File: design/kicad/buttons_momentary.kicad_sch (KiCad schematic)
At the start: 18 parts, among them J2 Conn_01x02_Socket, J3 Conn_01x02_Socket, J4 Conn_01x02_Socket, J5 Conn_01x02_Socket, J6 Conn_01x02_Socket, J7 Conn_01x02_Socket

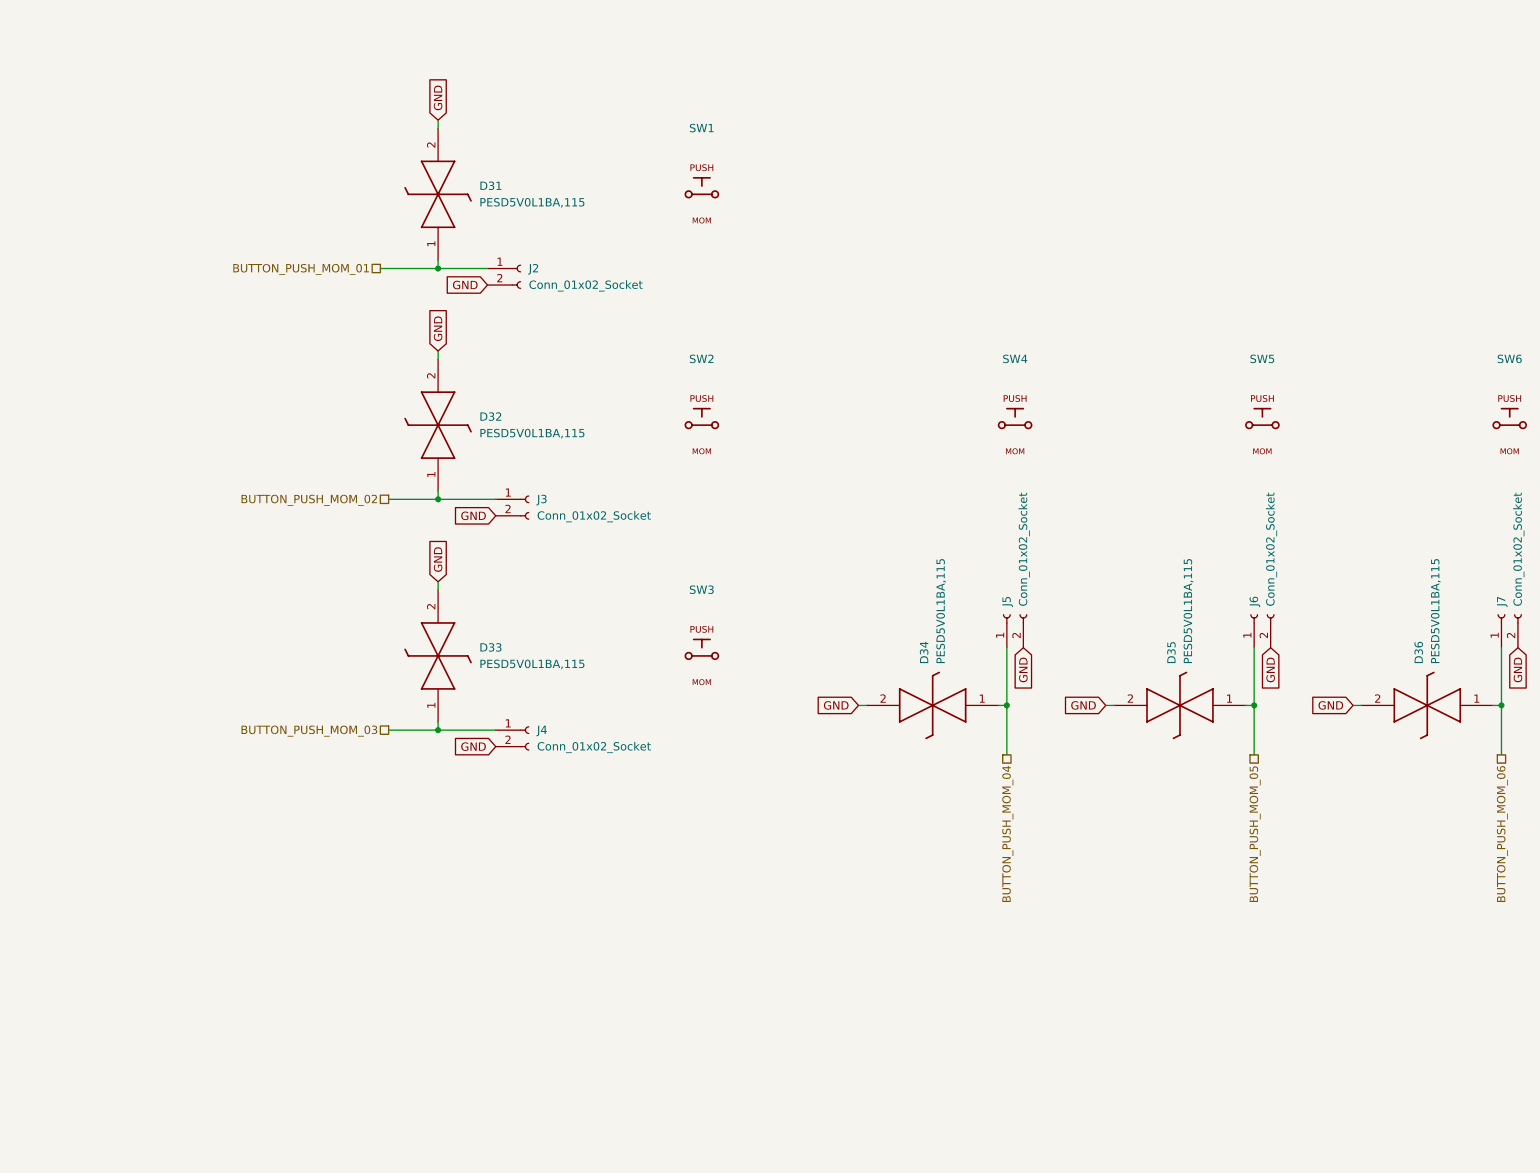
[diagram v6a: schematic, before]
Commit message: Fix net format name and update junctions in MIDI controller schematic
- Set net format name to "KiCad" in the project file.
- Added multiple junctions at specified coordinates in the schematic.
- Adjusted existing junction positions and UUIDs for consistency.
- Updated wire connections to reflect new junction placements.
- Corrected component references and properties for various components.
- Added new capacitor symbols with appropriate properties and references.
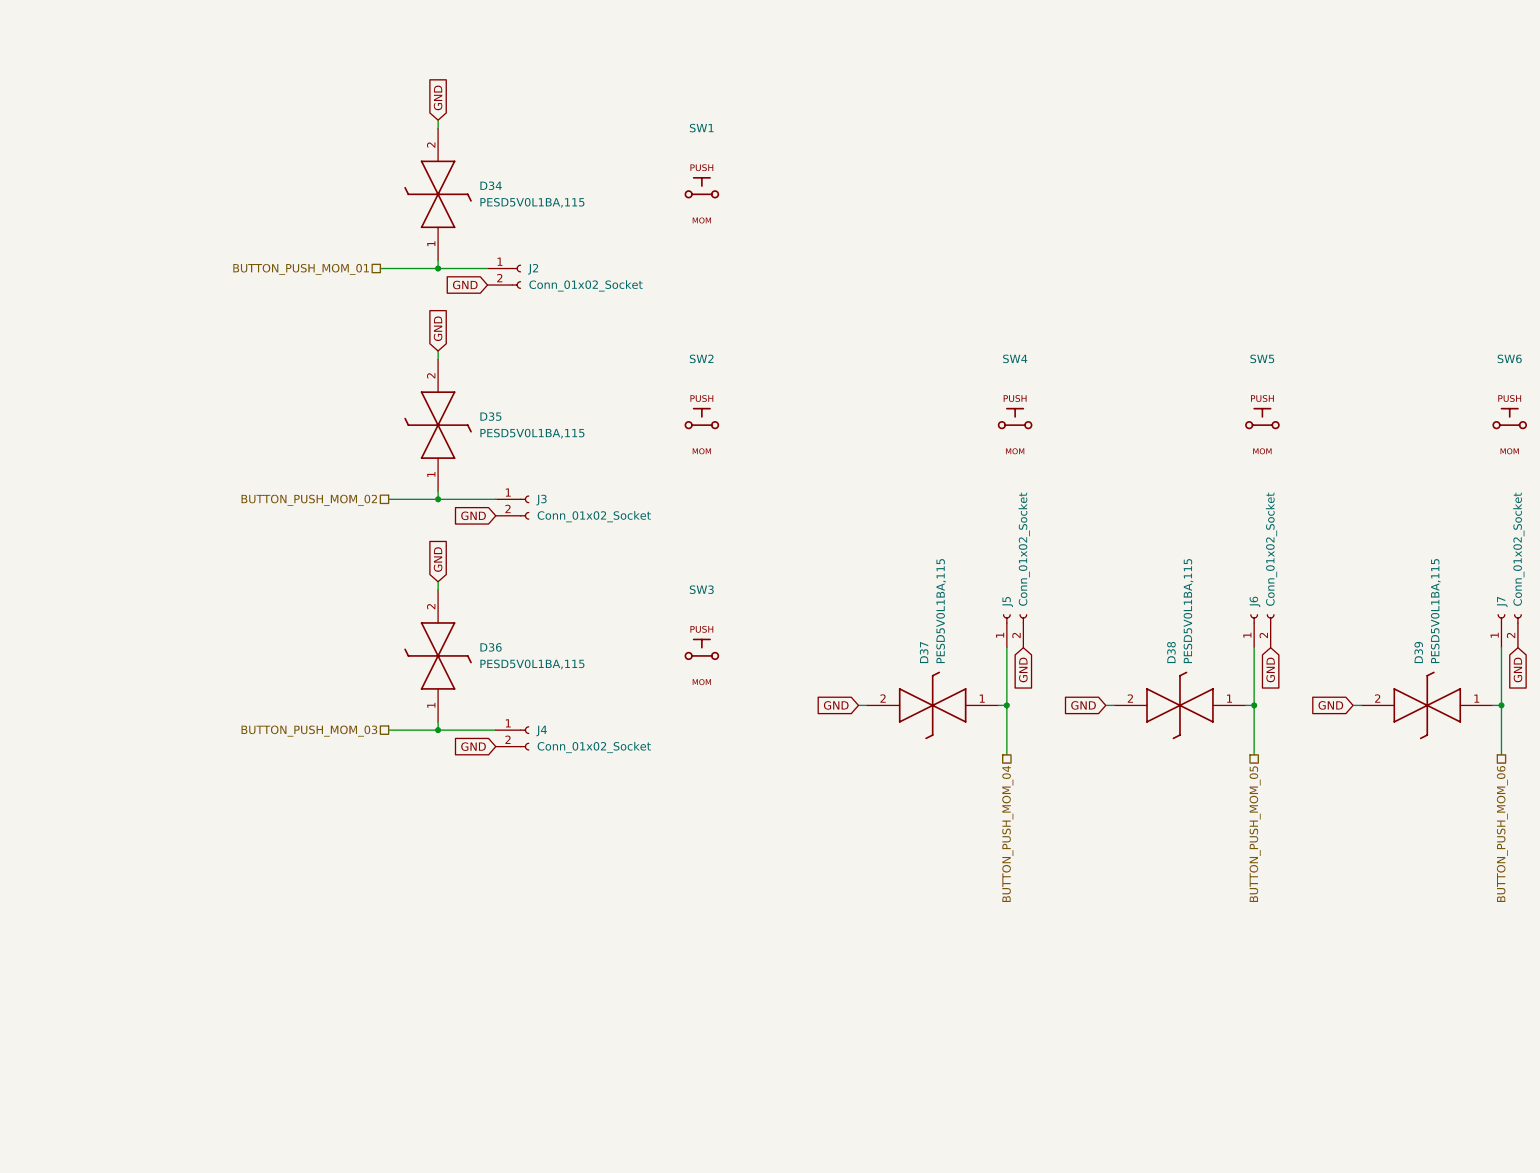
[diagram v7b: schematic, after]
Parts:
- renumbered D31 to D34, D32 to D35, D33 to D36, D34 to D37, D35 to D38, D36 to D39
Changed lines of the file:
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@@
 		(dnp no)
 		(fields_autoplaced yes)
-		(property "Reference" "D35"
+		(property "Reference" "D38"
 			(at 181.6099 114.3 90)
 			(effects
@@
 			(project "midi_controller"
 				(path "/9e44e663-00d0-4f33-bf1f-c4ad78deb554/9031f441-b35d-4c72-b3de-1ac6f4fd634b"
-					(reference "D35")
+					(reference "D38")
 					(unit 1)
 				)
@@
 		(dnp no)
 		(fields_autoplaced yes)
-		(property "Reference" "D32"
+		(property "Reference" "D35"
 			(at 74.93 76.1999 90)
 			(effects
@@
 			(project "midi_controller"
 				(path "/9e44e663-00d0-4f33-bf1f-c4ad78deb554/9031f441-b35d-4c72-b3de-1ac6f4fd634b"
-					(reference "D32")
+					(reference "D35")
 					(unit 1)
 				)
@@
 		(dnp no)
 		(fields_autoplaced yes)
-		(property "Reference" "D31"
+		(property "Reference" "D34"
 			(at 74.93 40.6399 90)
 			(effects
@@
 			(project "midi_controller"
 				(path "/9e44e663-00d0-4f33-bf1f-c4ad78deb554/9031f441-b35d-4c72-b3de-1ac6f4fd634b"
-					(reference "D31")
+					(reference "D34")
 					(unit 1)
 				)
@@
 		(dnp no)
 		(fields_autoplaced yes)
-		(property "Reference" "D34"
+		(property "Reference" "D37"
 			(at 143.5099 114.3 90)
 			(effects
@@
 			(project "midi_controller"
 				(path "/9e44e663-00d0-4f33-bf1f-c4ad78deb554/9031f441-b35d-4c72-b3de-1ac6f4fd634b"
-					(reference "D34")
+					(reference "D37")
 					(unit 1)
 				)
@@
 		(dnp no)
 		(fields_autoplaced yes)
-		(property "Reference" "D36"
+		(property "Reference" "D39"
 			(at 219.7099 114.3 90)
 			(effects
@@
 			(project "midi_controller"
 				(path "/9e44e663-00d0-4f33-bf1f-c4ad78deb554/9031f441-b35d-4c72-b3de-1ac6f4fd634b"
-					(reference "D36")
+					(reference "D39")
 					(unit 1)
 				)
@@
 		(dnp no)
 		(fields_autoplaced yes)
-		(property "Reference" "D33"
+		(property "Reference" "D36"
 			(at 74.93 111.7599 90)
 			(effects
@@
 			(project "midi_controller"
 				(path "/9e44e663-00d0-4f33-bf1f-c4ad78deb554/9031f441-b35d-4c72-b3de-1ac6f4fd634b"
-					(reference "D33")
-					(unit 1)
-				)
+					(reference "D36")
+					(unit 1)
+				)

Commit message: Fix reference labels and update wire connections in MIDI controller and multiplexer schematics
- Adjusted wire connection points in the MIDI controller schematic for better alignment.
- Updated label positions for various components in the MIDI controller schematic.
- Renamed reference designators for capacitors and power connections in the multiplexer schematic to maintain consistency.
- Corrected the reference designators for multiple components to reflect accurate labeling.
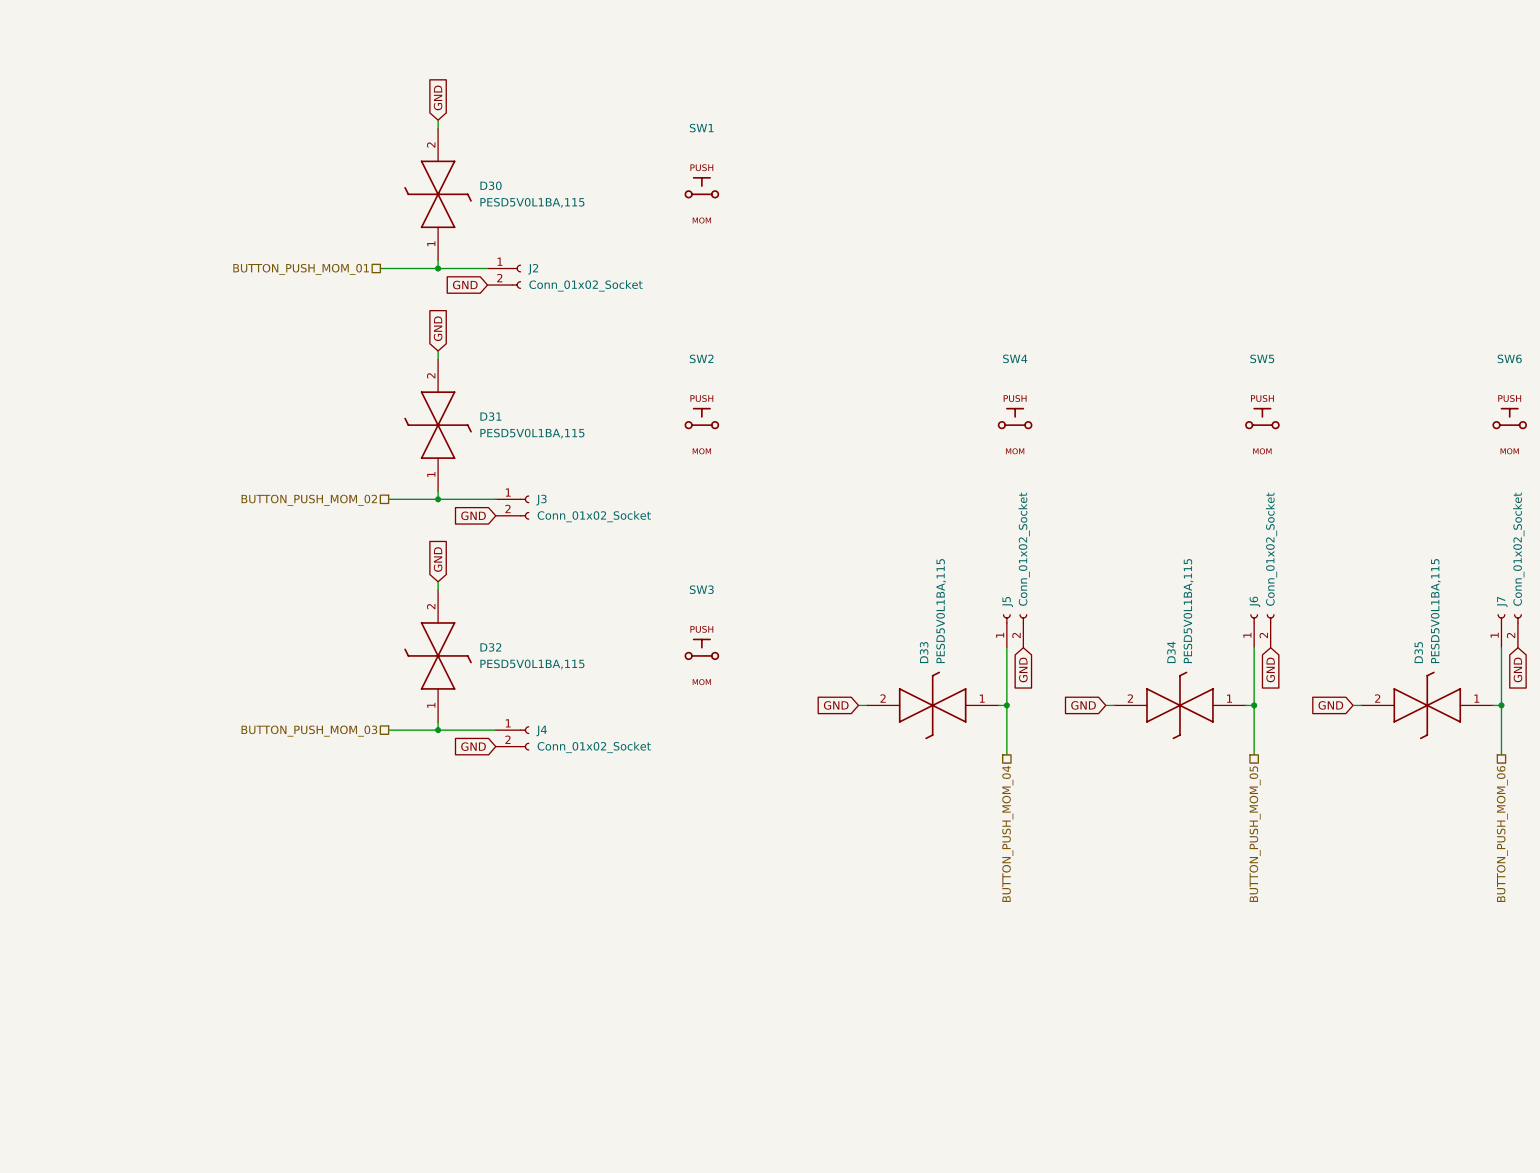
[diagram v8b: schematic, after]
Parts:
- renumbered D34 to D30, D35 to D31, D36 to D32, D37 to D33, D38 to D34, D39 to D35
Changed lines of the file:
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@@
 		(dnp no)
 		(fields_autoplaced yes)
-		(property "Reference" "D38"
+		(property "Reference" "D34"
 			(at 181.6099 114.3 90)
 			(effects
@@
 			(project "midi_controller"
 				(path "/9e44e663-00d0-4f33-bf1f-c4ad78deb554/9031f441-b35d-4c72-b3de-1ac6f4fd634b"
-					(reference "D38")
+					(reference "D34")
 					(unit 1)
 				)
@@
 		(dnp no)
 		(fields_autoplaced yes)
-		(property "Reference" "D35"
+		(property "Reference" "D31"
 			(at 74.93 76.1999 90)
 			(effects
@@
 			(project "midi_controller"
 				(path "/9e44e663-00d0-4f33-bf1f-c4ad78deb554/9031f441-b35d-4c72-b3de-1ac6f4fd634b"
-					(reference "D35")
+					(reference "D31")
 					(unit 1)
 				)
@@
 		(dnp no)
 		(fields_autoplaced yes)
-		(property "Reference" "D34"
+		(property "Reference" "D30"
 			(at 74.93 40.6399 90)
 			(effects
@@
 			(project "midi_controller"
 				(path "/9e44e663-00d0-4f33-bf1f-c4ad78deb554/9031f441-b35d-4c72-b3de-1ac6f4fd634b"
-					(reference "D34")
+					(reference "D30")
 					(unit 1)
 				)
@@
 		(dnp no)
 		(fields_autoplaced yes)
-		(property "Reference" "D37"
+		(property "Reference" "D33"
 			(at 143.5099 114.3 90)
 			(effects
@@
 			(project "midi_controller"
 				(path "/9e44e663-00d0-4f33-bf1f-c4ad78deb554/9031f441-b35d-4c72-b3de-1ac6f4fd634b"
-					(reference "D37")
+					(reference "D33")
 					(unit 1)
 				)
@@
 		(dnp no)
 		(fields_autoplaced yes)
-		(property "Reference" "D39"
+		(property "Reference" "D35"
 			(at 219.7099 114.3 90)
 			(effects
@@
 			(project "midi_controller"
 				(path "/9e44e663-00d0-4f33-bf1f-c4ad78deb554/9031f441-b35d-4c72-b3de-1ac6f4fd634b"
-					(reference "D39")
+					(reference "D35")
 					(unit 1)
 				)
@@
 		(dnp no)
 		(fields_autoplaced yes)
-		(property "Reference" "D36"
+		(property "Reference" "D32"
 			(at 74.93 111.7599 90)
 			(effects
@@
 			(project "midi_controller"
 				(path "/9e44e663-00d0-4f33-bf1f-c4ad78deb554/9031f441-b35d-4c72-b3de-1ac6f4fd634b"
-					(reference "D36")
-					(unit 1)
-				)
+					(reference "D32")
+					(unit 1)
+				)
